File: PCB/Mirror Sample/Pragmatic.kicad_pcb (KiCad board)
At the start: 2 copper layers, 13 parts, among them J1 Conn_02x08_Odd_Even, SW1 SW_Push, SW2 SW_Push, SW7 SW_Push, SW8 SW_Push

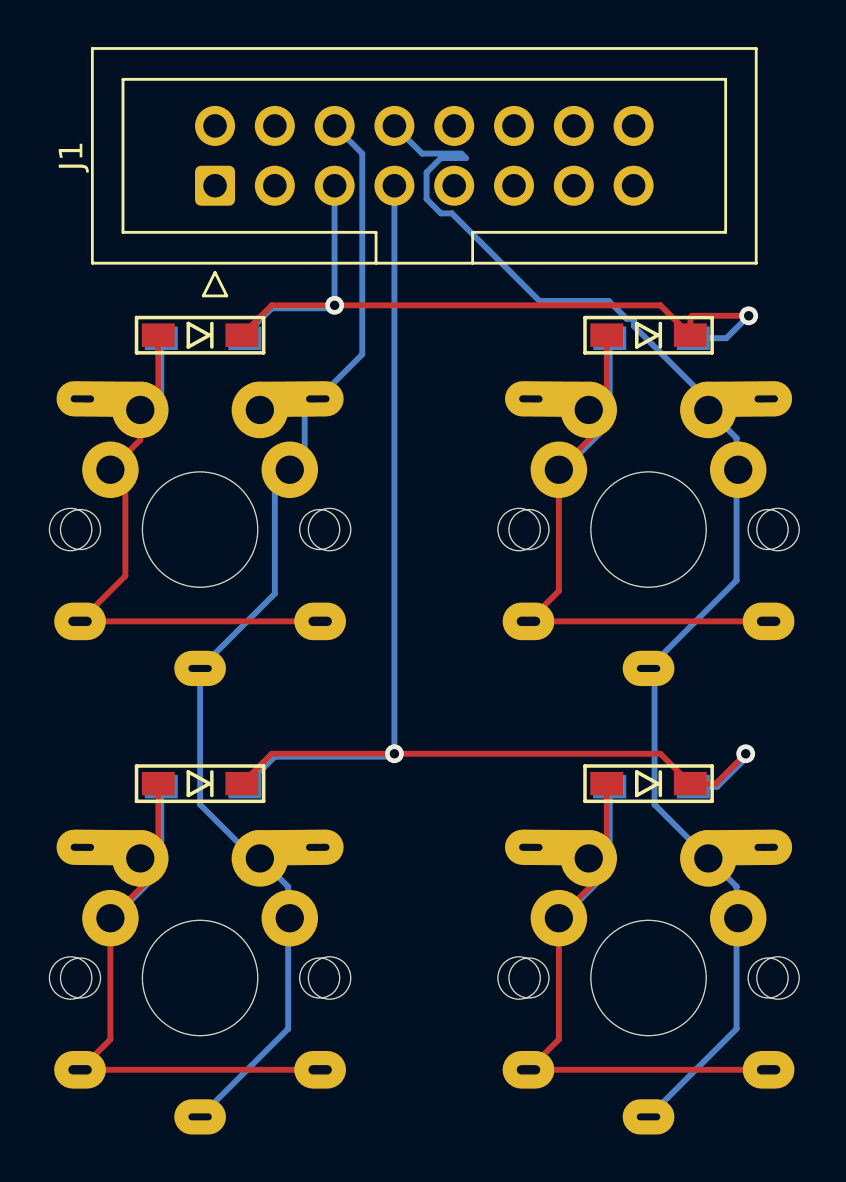
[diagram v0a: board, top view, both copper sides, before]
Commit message: fix schematic to PCB problem。
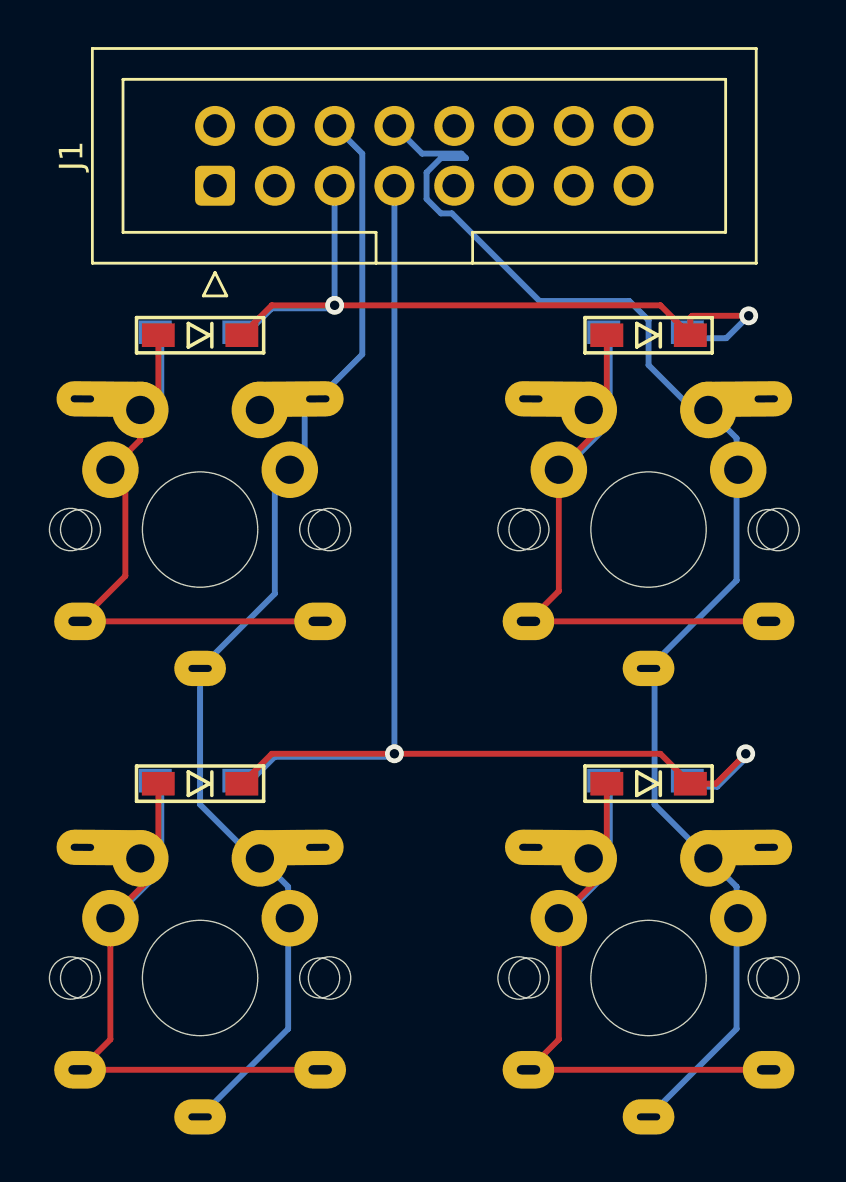
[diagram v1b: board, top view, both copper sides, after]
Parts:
- removed the D1 at (57.3, 49.0)
- removed the D2 at (76.3, 49.0)
- removed the D7 at (57.3, 68.1)
- removed the D8 at (76.3, 68.1)
- D1, D2, D7, D8: footprint Foostan:D3_SMD_v2 -> Pragmatic:D_SMD
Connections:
- J1 pad 11: (no net) -> Row4
- J1 pad 12: (no net) -> Col4
- J1 pad 13: (no net) -> Row5
- J1 pad 14: (no net) -> Col5
- J1 pad 15: (no net) -> Row6
- J1 pad 16: (no net) -> Col6
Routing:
- net Col2: track 57.9 -> 58.6 mm
